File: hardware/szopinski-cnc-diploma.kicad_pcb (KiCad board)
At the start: 2 copper layers, 99.1 x 62.2 mm, 30 parts, among them J1 Barrel_Jack, J2 Conn_02x08_Odd_Even, J3 AVR-ISP-10, J4 Conn_01x04, J5 Conn_01x04, J6 Conn_01x04, J7 Conn_01x04, U1 ATmega328P-PU, U2 L7805, U3 DRV8825, U4 DRV8825, U5 DRV8825, U6 DRV8825, Y1 20 MHz

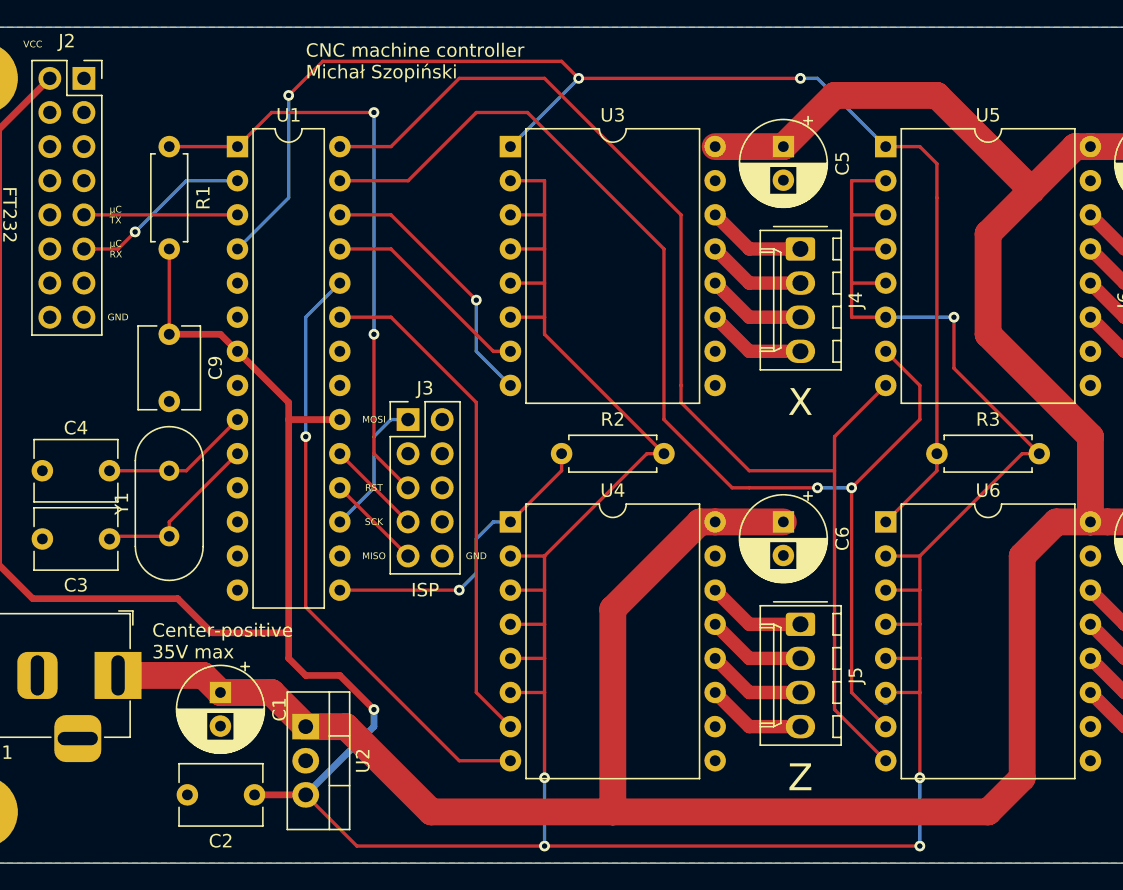
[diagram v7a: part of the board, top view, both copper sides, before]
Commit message: Fix trace widths and PCB layout
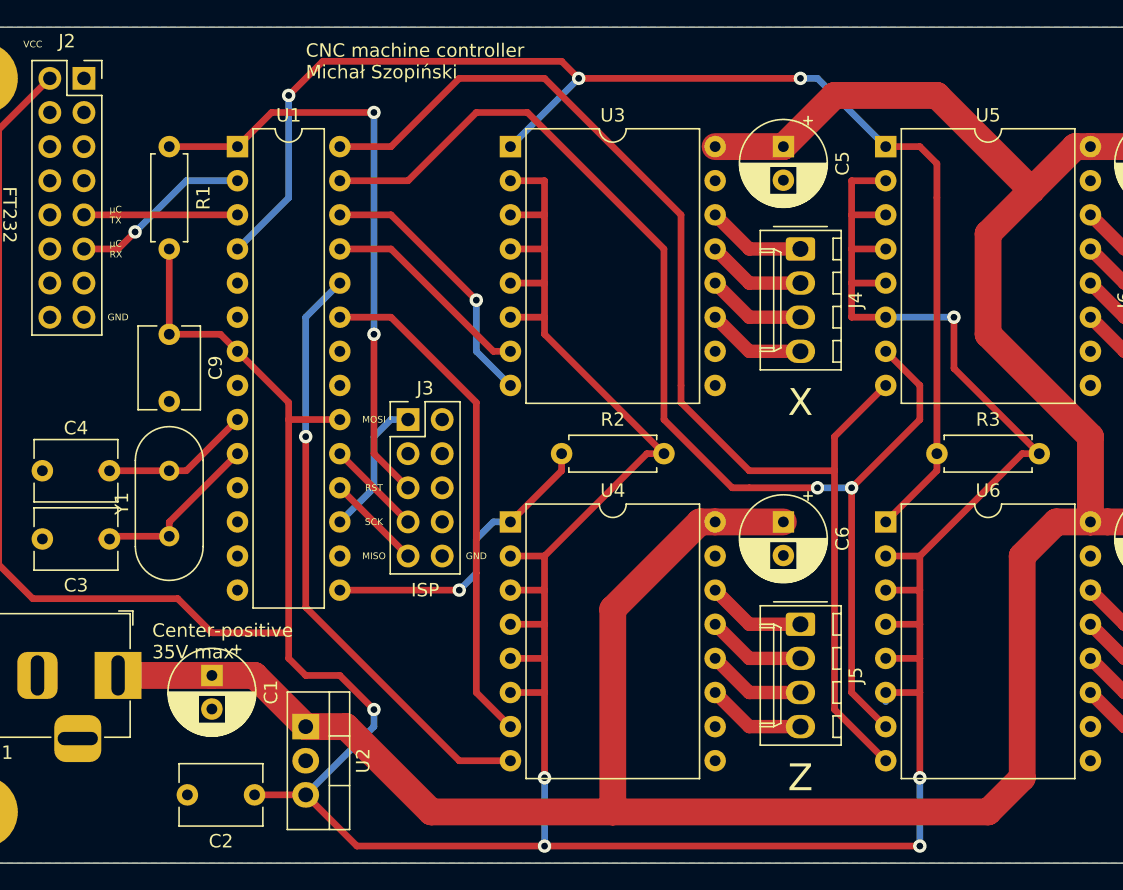
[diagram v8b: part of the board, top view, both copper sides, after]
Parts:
- moved C1 1.42 mm to (126.4, 128.3)
